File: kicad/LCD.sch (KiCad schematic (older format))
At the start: 9 parts, among them J4 Conn_02x20_Odd_Even, U21 74LVC4245A, U22 74LVC244A

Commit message: SDcard interface mostly complete.
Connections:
- net GND: no longer U22.11 (2A3), U22.13 (2A2)
- net SDCLK_3V3: now reaches U22.7 (2Y2)
- net ~SDCS_3V3: now reaches U22.9 (2Y3)
- new net SDCLK_5V: U22.13 (2A2)
- new net ~SDCS_5V: U22.11 (2A3)
- no-connect marks 13 -> 11
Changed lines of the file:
@@
 	1    0    0    -1
 $EndComp
-NoConn ~ 6550 3550
-NoConn ~ 6550 3450
 Wire Wire Line
 	5550 2850 5350 2850
@@
 	5350 2850 2000 2850
 Wire Wire Line
-	5550 3450 5550 3550
-Wire Wire Line
-	5550 3550 5550 3750
-Connection ~ 5550 3550
-Wire Wire Line
 	5550 3750 5550 3850
-Connection ~ 5550 3750
 Connection ~ 5550 3850
 Wire Wire Line
@@
 Wire Wire Line
 	5550 3350 2000 3350
+Text GLabel 5100 3450 0    60   Input ~ 0
+SDCLK_5V
+Text GLabel 5100 3600 0    60   Input ~ 0
+~SDCS_5V
+Wire Wire Line
+	5100 3450 5550 3450
+Wire Wire Line
+	5100 3600 5550 3600
+Wire Wire Line
+	5550 3600 5550 3550
+Text GLabel 7000 3450 2    60   Output ~ 0
+SDCLK_3V3
+Text GLabel 7000 3600 2    60   Output ~ 0
+~SDCS_3V3
+Wire Wire Line
+	6550 3450 7000 3450
+Wire Wire Line
+	6550 3550 6550 3600
+Wire Wire Line
+	6550 3600 7000 3600
 Wire Bus Line
 	5200 1300 5200 2000

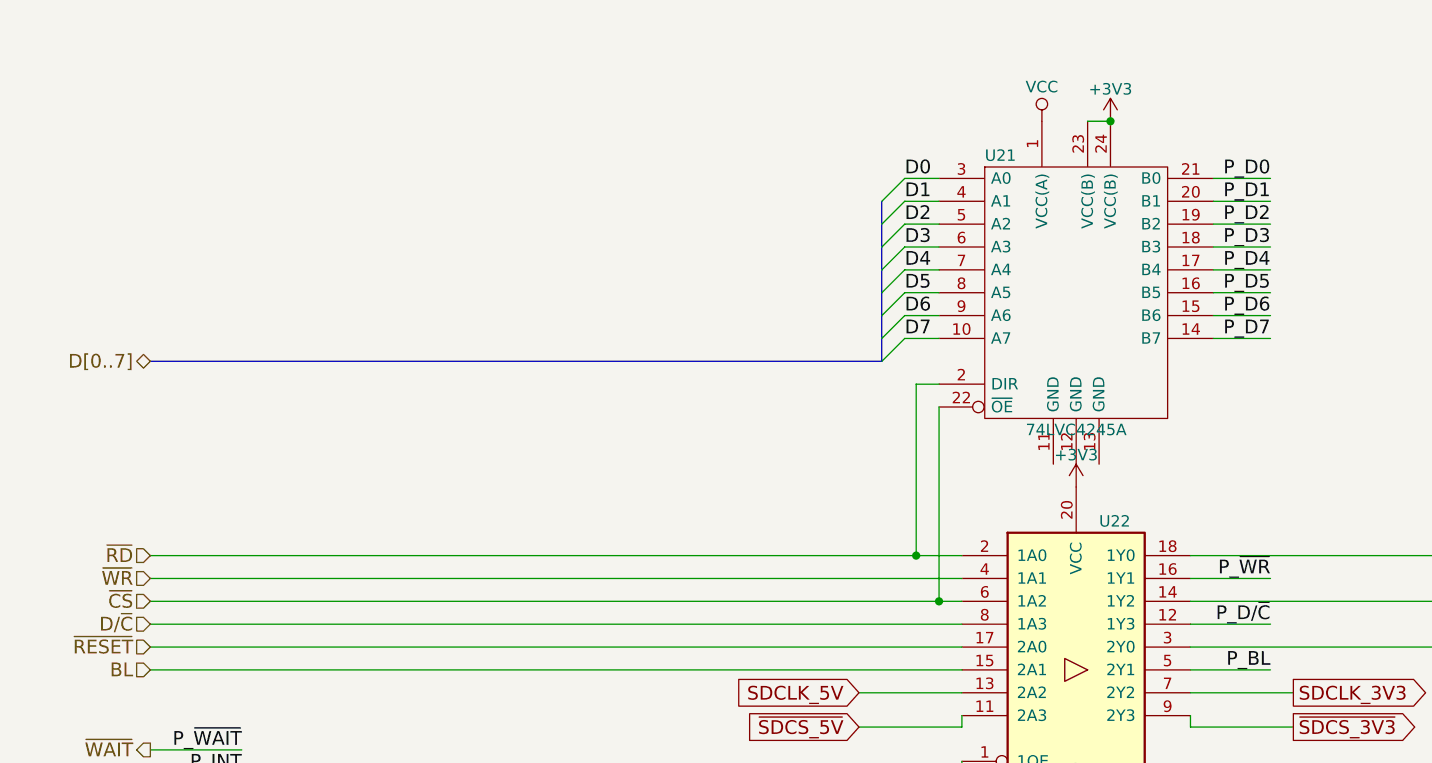
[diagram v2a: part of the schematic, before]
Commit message: Add audio output.
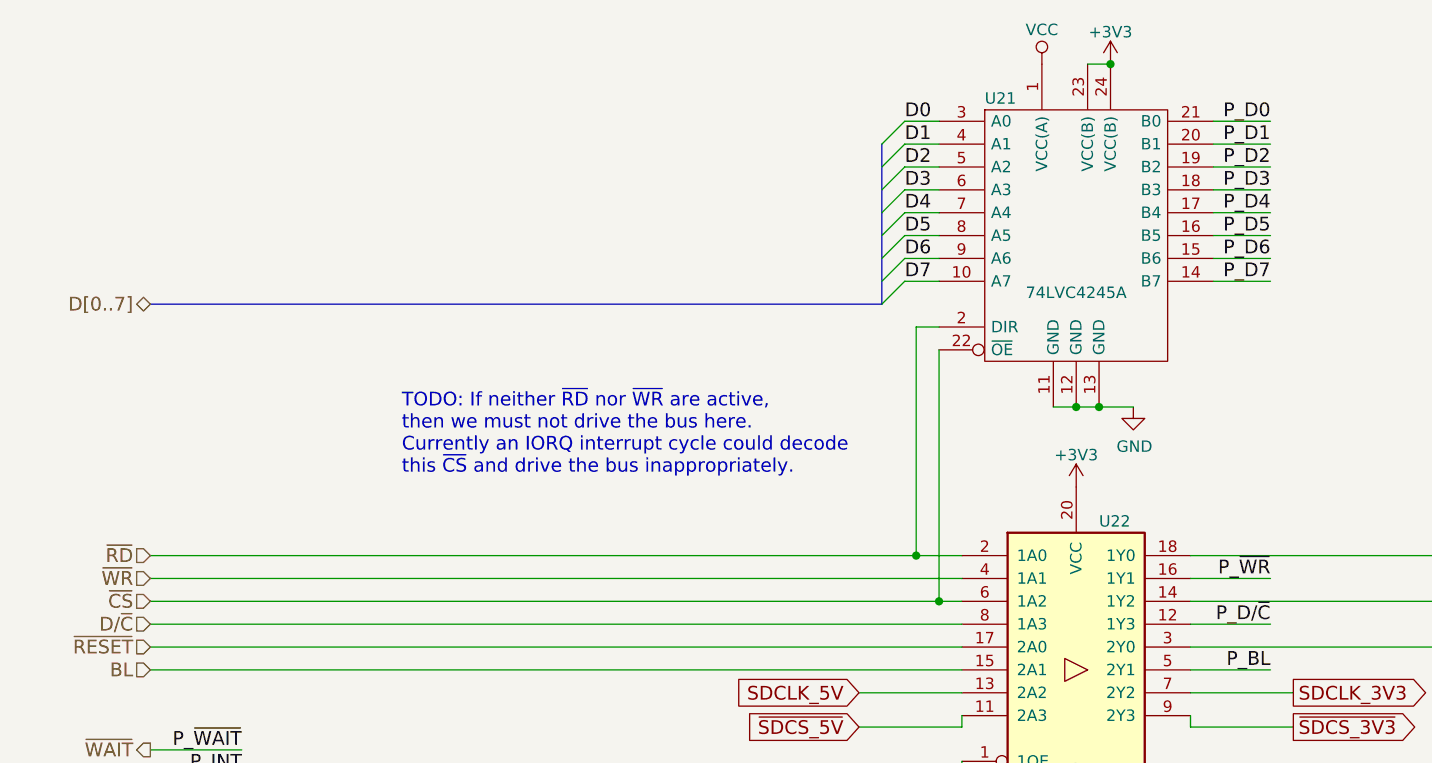
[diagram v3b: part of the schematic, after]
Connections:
- net GND: now also U21.11 (GND), U21.12 (GND), U21.13 (GND)
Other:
- note added: "TODO: If neither ~RD~ nor ~WR~ are active,\nthen we must not drive the bus here. \nCurrently an IORQ interrupt cycle could decode\nthis ~CS~ and drive the bus inappropriately."
- moved on the sheet: U21
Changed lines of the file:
@@
 EESchema Schematic File Version 4
 LIBS:z80-cache
-EELAYER 26 0
+EELAYER 29 0
 EELAYER END
 $Descr USLetter 11000 8500
 encoding utf-8
-Sheet 8 10
+Sheet 8 11
 Title "LCD Interface"
 Date "2018-07-20"
@@
 	1    0    0    -1
 $EndComp
-Text HLabel 2000 2000 0    60   BiDi ~ 0
+Text HLabel 2000 1750 0    60   BiDi ~ 0
 D[0..7]
 Text HLabel 2000 2850 0    60   Input ~ 0
@@
 L power:VCC #PWR086
 U 1 1 5B4E19BB
-P 5900 950
-F 0 "#PWR086" H 5900 800 50  0001 C CNN
-F 1 "VCC" H 5900 1100 50  0000 C CNN
-F 2 "" H 5900 950 50  0001 C CNN
-F 3 "" H 5900 950 50  0001 C CNN
-	1    5900 950
+P 5900 700
+F 0 "#PWR086" H 5900 550 50  0001 C CNN
+F 1 "VCC" H 5900 850 50  0000 C CNN
+F 2 "" H 5900 700 50  0001 C CNN
+F 3 "" H 5900 700 50  0001 C CNN
+	1    5900 700
 	1    0    0    -1
 $EndComp
@@
 L power:+3V3 #PWR087
 U 1 1 5B4E19D3
-P 6200 950
-F 0 "#PWR087" H 6200 800 50  0001 C CNN
-F 1 "+3V3" H 6200 1090 50  0000 C CNN
-F 2 "" H 6200 950 50  0001 C CNN
-F 3 "" H 6200 950 50  0001 C CNN
-	1    6200 950
-	1    0    0    -1
-$EndComp
-Wire Wire Line
-	6100 950  6200 950
-Connection ~ 6200 950
+P 6200 700
+F 0 "#PWR087" H 6200 550 50  0001 C CNN
+F 1 "+3V3" H 6200 840 50  0000 C CNN
+F 2 "" H 6200 700 50  0001 C CNN
+F 3 "" H 6200 700 50  0001 C CNN
+	1    6200 700
+	1    0    0    -1
+$EndComp
+Wire Wire Line
+	6100 700  6200 700
+Connection ~ 6200 700
 Wire Bus Line
-	5200 2000 2000 2000
+	5200 1750 2000 1750
 $Comp
 L headquarters:74LVC4245A U21
 U 1 1 5B4E22A0
-P 6050 1700
-F 0 "U21" H 5650 2300 50  0000 L CNN
-F 1 "74LVC4245A" H 6050 1100 50  0000 C CNN
-F 2 "" H 6050 1700 50  0001 C CNN
-F 3 "" H 6050 1700 50  0001 C CNN
-	1    6050 1700
-	1    0    0    -1
-$EndComp
-Wire Wire Line
-	5450 1200 5300 1200
-Wire Wire Line
-	5450 1300 5300 1300
-Wire Wire Line
-	5450 1400 5300 1400
-Wire Wire Line
-	5450 1500 5300 1500
-Wire Wire Line
-	5450 1600 5300 1600
-Wire Wire Line
-	5450 1700 5300 1700
-Wire Wire Line
-	5450 1800 5300 1800
-Wire Wire Line
-	5450 1900 5300 1900
-Text Label 5300 1200 0    60   ~ 0
+P 6050 1450
+F 0 "U21" H 5650 2050 50  0000 L CNN
+F 1 "74LVC4245A" H 6050 1200 50  0000 C CNN
+F 2 "" H 6050 1450 50  0001 C CNN
+F 3 "" H 6050 1450 50  0001 C CNN
+	1    6050 1450
+	1    0    0    -1
+$EndComp
+Wire Wire Line
+	5450 950  5300 950
+Wire Wire Line
+	5450 1050 5300 1050
+Wire Wire Line
+	5450 1150 5300 1150
+Wire Wire Line
+	5450 1250 5300 1250
+Wire Wire Line
+	5450 1350 5300 1350
+Wire Wire Line
+	5450 1450 5300 1450
+Wire Wire Line
+	5450 1550 5300 1550
+Wire Wire Line
+	5450 1650 5300 1650
+Text Label 5300 950  0    60   ~ 0
 D0
-Text Label 5300 1300 0    60   ~ 0
+Text Label 5300 1050 0    60   ~ 0
 D1
-Text Label 5300 1400 0    60   ~ 0
+Text Label 5300 1150 0    60   ~ 0
 D2
-Text Label 5300 1500 0    60   ~ 0
+Text Label 5300 1250 0    60   ~ 0
 D3
-Text Label 5300 1600 0    60   ~ 0
+Text Label 5300 1350 0    60   ~ 0
 D4
-Text Label 5300 1700 0    60   ~ 0
+Text Label 5300 1450 0    60   ~ 0
 D5
-Text Label 5300 1800 0    60   ~ 0
+Text Label 5300 1550 0    60   ~ 0
 D6
-Text Label 5300 1900 0    60   ~ 0
+Text Label 5300 1650 0    60   ~ 0
 D7
 Entry Wire Line
-	5200 1300 5300 1200
-Entry Wire Line
-	5200 1400 5300 1300
-Entry Wire Line
-	5200 1500 5300 1400
-Entry Wire Line
-	5200 1600 5300 1500
-Entry Wire Line
-	5200 1700 5300 1600
-Entry Wire Line
-	5200 1800 5300 1700
-Entry Wire Line
-	5200 1900 5300 1800
-Entry Wire Line
-	5200 2000 5300 1900
-Wire Wire Line
-	6650 1200 6900 1200
-Wire Wire Line
-	6650 1300 6900 1300
-Wire Wire Line
-	6650 1400 6900 1400
-Wire Wire Line
-	6650 1500 6900 1500
-Wire Wire Line
-	6650 1600 6900 1600
-Wire Wire Line
-	6650 1700 6900 1700
-Wire Wire Line
-	6650 1800 6900 1800
-Wire Wire Line
-	6650 1900 6900 1900
-Text Label 6900 1200 2    60   ~ 0
+	5200 1050 5300 950
+Entry Wire Line
+	5200 1150 5300 1050
+Entry Wire Line
+	5200 1250 5300 1150
+Entry Wire Line
+	5200 1350 5300 1250
+Entry Wire Line
+	5200 1450 5300 1350
+Entry Wire Line
+	5200 1550 5300 1450
+Entry Wire Line
+	5200 1650 5300 1550
+Entry Wire Line
+	5200 1750 5300 1650
+Wire Wire Line
+	6650 950  6900 950
+Wire Wire Line
+	6650 1050 6900 1050
+Wire Wire Line
+	6650 1150 6900 1150
+Wire Wire Line
+	6650 1250 6900 1250
+Wire Wire Line
+	6650 1350 6900 1350
+Wire Wire Line
+	6650 1450 6900 1450
+Wire Wire Line
+	6650 1550 6900 1550
+Wire Wire Line
+	6650 1650 6900 1650
+Text Label 6900 950  2    60   ~ 0
 P_D0
-Text Label 6900 1300 2    60   ~ 0
+Text Label 6900 1050 2    60   ~ 0
 P_D1
-Text Label 6900 1400 2    60   ~ 0
+Text Label 6900 1150 2    60   ~ 0
 P_D2
-Text Label 6900 1500 2    60   ~ 0
+Text Label 6900 1250 2    60   ~ 0
 P_D3
-Text Label 6900 1600 2    60   ~ 0
+Text Label 6900 1350 2    60   ~ 0
 P_D4
-Text Label 6900 1700 2    60   ~ 0
+Text Label 6900 1450 2    60   ~ 0
 P_D5
-Text Label 6900 1800 2    60   ~ 0
+Text Label 6900 1550 2    60   ~ 0
 P_D6
-Text Label 6900 1900 2    60   ~ 0
+Text Label 6900 1650 2    60   ~ 0
 P_D7
 Text Notes 10150 2300 2    60   ~ 0
@@
 $EndComp
 Wire Wire Line
-	5550 2850 5350 2850
-Wire Wire Line
 	2000 2950 5550 2950
 Wire Wire Line
-	2000 3050 5450 3050
-Wire Wire Line
 	2000 3150 5550 3150
 Wire Wire Line
 	2000 3250 5550 3250
 Wire Wire Line
-	5450 2200 5450 3050
-Connection ~ 5450 3050
-Wire Wire Line
-	5450 2100 5350 2100
-Wire Wire Line
-	5350 2100 5350 2850
-Connection ~ 5350 2850
+	5450 1850 5350 1850
 Wire Wire Line
 	7900 2950 9400 2950
@@
 	9400 4750 9900 4750
 Wire Wire Line
-	5450 3050 5550 3050
-Wire Wire Line
-	5350 2850 2000 2850
-Wire Wire Line
 	5550 3750 5550 3850
 Connection ~ 5550 3850
@@
 Wire Wire Line
 	6550 3600 7000 3600
+Wire Wire Line
+	2000 2850 5350 2850
+Wire Wire Line
+	2000 3050 5450 3050
+Wire Wire Line
+	5450 1950 5450 3050
+Connection ~ 5450 3050
+Wire Wire Line
+	5450 3050 5550 3050
+Wire Wire Line
+	5350 1850 5350 2850
+Connection ~ 5350 2850
+Wire Wire Line
+	5350 2850 5550 2850
+$Comp
+L power:GND #PWR0141
+U 1 1 5CC16D4B
+P 6300 2200
+F 0 "#PWR0141" H 6300 1950 50  0001 C CNN
+F 1 "GND" H 6305 2027 50  0000 C CNN
+F 2 "" H 6300 2200 50  0001 C CNN
+F 3 "" H 6300 2200 50  0001 C CNN
+	1    6300 2200
+	1    0    0    -1
+$EndComp
+Wire Wire Line
+	5950 2200 6050 2200
+Wire Wire Line
+	6050 2200 6150 2200
+Connection ~ 6050 2200
+Wire Wire Line
+	6150 2200 6300 2200
+Connection ~ 6150 2200
 Wire Bus Line
-	5200 1300 5200 2000
+	5200 1050 5200 1750
+Text Notes 3100 2500 0    60   ~ 0
+TODO: If neither ~RD~ nor ~WR~ are active,\nthen we must not drive the bus here. \nCurrently an IORQ interrupt cycle could decode\nthis ~CS~ and drive the bus inappropriately.
 $EndSCHEMATC

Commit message: First complete version of ZED-80 schematic.
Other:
- note added: "If neither ~RD~ nor ~WR~ are active,\nthen we must not drive the Z80 data bus. \nAn IORQ interrupt cycle could drive\nthis ~CS~ active, enabling transceiver outputs.\nWe’re okay because ~RD~ will be inactive, so\nDIR will be high, making the A side inputs, and\nthe B side outputs."
- note removed: "TODO: If neither ~RD~ nor ~WR~ are active,\nthen we must not drive the bus here. \nCurrently an IORQ interrupt cycle could decode\nthis ~CS~ and drive the bus inappropriately."
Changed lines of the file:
@@
 EESchema Schematic File Version 4
-LIBS:z80-cache
 EELAYER 29 0
 EELAYER END
@@
 Sheet 8 11
 Title "LCD Interface"
-Date "2018-07-20"
-Rev "12"
+Date "2019-04-03"
+Rev "1"
 Comp ""
 Comment1 ""
@@
 	6150 2200 6300 2200
 Connection ~ 6150 2200
+Text Notes 2800 1500 0    60   ~ 0
+If neither ~RD~ nor ~WR~ are active,\nthen we must not drive the Z80 data bus. \nAn IORQ interrupt cycle could drive\nthis ~CS~ active, enabling transceiver outputs.\nWe’re okay because ~RD~ will be inactive, so\nDIR will be high, making the A side inputs, and\nthe B side outputs.
 Wire Bus Line
 	5200 1050 5200 1750
-Text Notes 3100 2500 0    60   ~ 0
-TODO: If neither ~RD~ nor ~WR~ are active,\nthen we must not drive the bus here. \nCurrently an IORQ interrupt cycle could decode\nthis ~CS~ and drive the bus inappropriately.
 $EndSCHEMATC

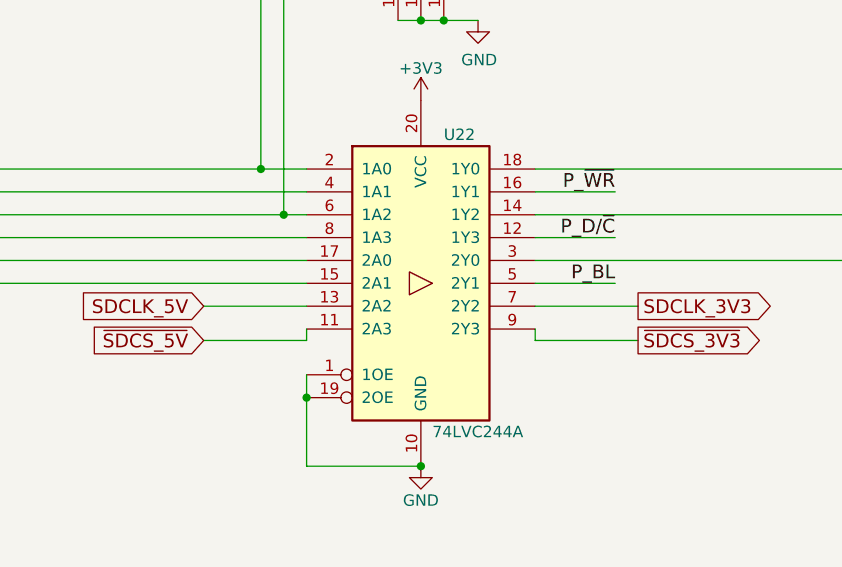
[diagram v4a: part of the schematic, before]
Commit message: Assign footprints.
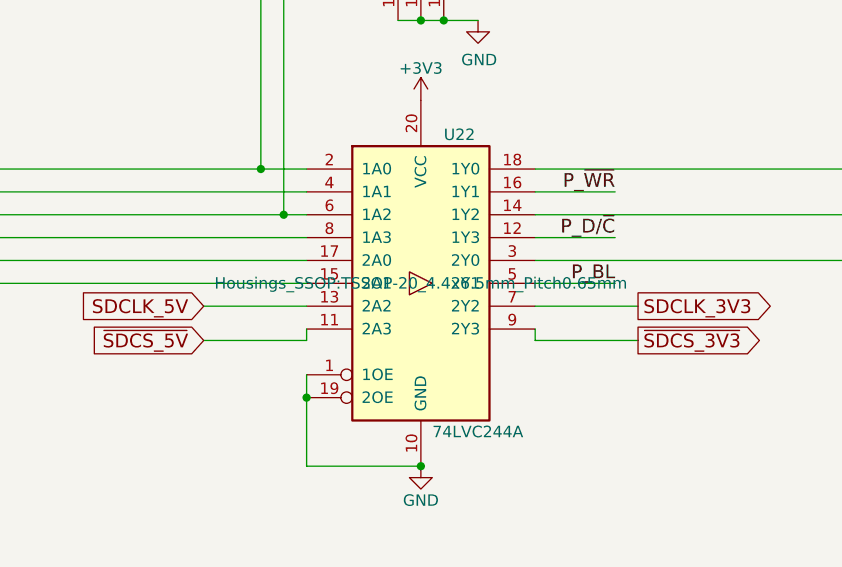
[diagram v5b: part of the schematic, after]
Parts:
- J4: footprint (none) -> Pin_Headers:Pin_Header_Straight_2x20_Pitch2.54mm
- R32: footprint (none) -> Resistors_SMD:R_0805_HandSoldering
- U21: footprint (none) -> Housings_SSOP:TSSOP-24_4.4x7.8mm_Pitch0.65mm
- U22: footprint (none) -> Housings_SSOP:TSSOP-20_4.4x6.5mm_Pitch0.65mm
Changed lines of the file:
@@
 F 0 "J4" H 9650 4550 50  0000 C CNN
 F 1 "Conn_02x20_Odd_Even" H 9650 2450 50  0000 C CNN
-F 2 "" H 9600 3550 50  0001 C CNN
+F 2 "Pin_Headers:Pin_Header_Straight_2x20_Pitch2.54mm" H 9600 3550 50  0001 C CNN
 F 3 "" H 9600 3550 50  0001 C CNN
 	1    9600 3550
@@
 F 0 "U21" H 5650 2050 50  0000 L CNN
 F 1 "74LVC4245A" H 6050 1200 50  0000 C CNN
-F 2 "" H 6050 1450 50  0001 C CNN
+F 2 "Housings_SSOP:TSSOP-24_4.4x7.8mm_Pitch0.65mm" H 6050 1450 50  0001 C CNN
 F 3 "" H 6050 1450 50  0001 C CNN
 	1    6050 1450
@@
 F 0 "U22" H 6150 4000 50  0000 L CNN
 F 1 "74LVC244A" H 6100 2700 50  0000 L CNN
-F 2 "" H 6050 3350 50  0000 C CNN
+F 2 "Housings_SSOP:TSSOP-20_4.4x6.5mm_Pitch0.65mm" H 6050 3350 50  0000 C CNN
 F 3 "" H 6050 3350 50  0000 C CNN
 	1    6050 3350
@@
 F 0 "R32" V 8430 3150 50  0000 C CNN
 F 1 "10K" V 8350 3150 50  0000 C CNN
-F 2 "" V 8280 3150 50  0001 C CNN
+F 2 "Resistors_SMD:R_0805_HandSoldering" V 8280 3150 50  0001 C CNN
 F 3 "" H 8350 3150 50  0001 C CNN
 	1    8350 3150
